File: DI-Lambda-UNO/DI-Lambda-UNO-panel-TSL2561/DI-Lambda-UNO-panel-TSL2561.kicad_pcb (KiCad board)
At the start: 2 copper layers, 33.2 x 26.6 mm, 3 parts, among them J1 Conn_01X06, U1 TSL2561

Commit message: Fix spring contact module name
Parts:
- J1: footprint Sprint-contact-connector-2:Contact-2.5x6 -> Spring-contact-connector-2:Contact-2.5x6
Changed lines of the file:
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@@
     )
   )
-  (module Sprint-contact-connector-2:Contact-2.5x6 (layer F.Cu)
+  (module Spring-contact-connector-2:Contact-2.5x6 (layer F.Cu)
     (at 160 90.7)
     (fp_text reference J1 (at -0.6 0.1) (layer F.SilkS) hide

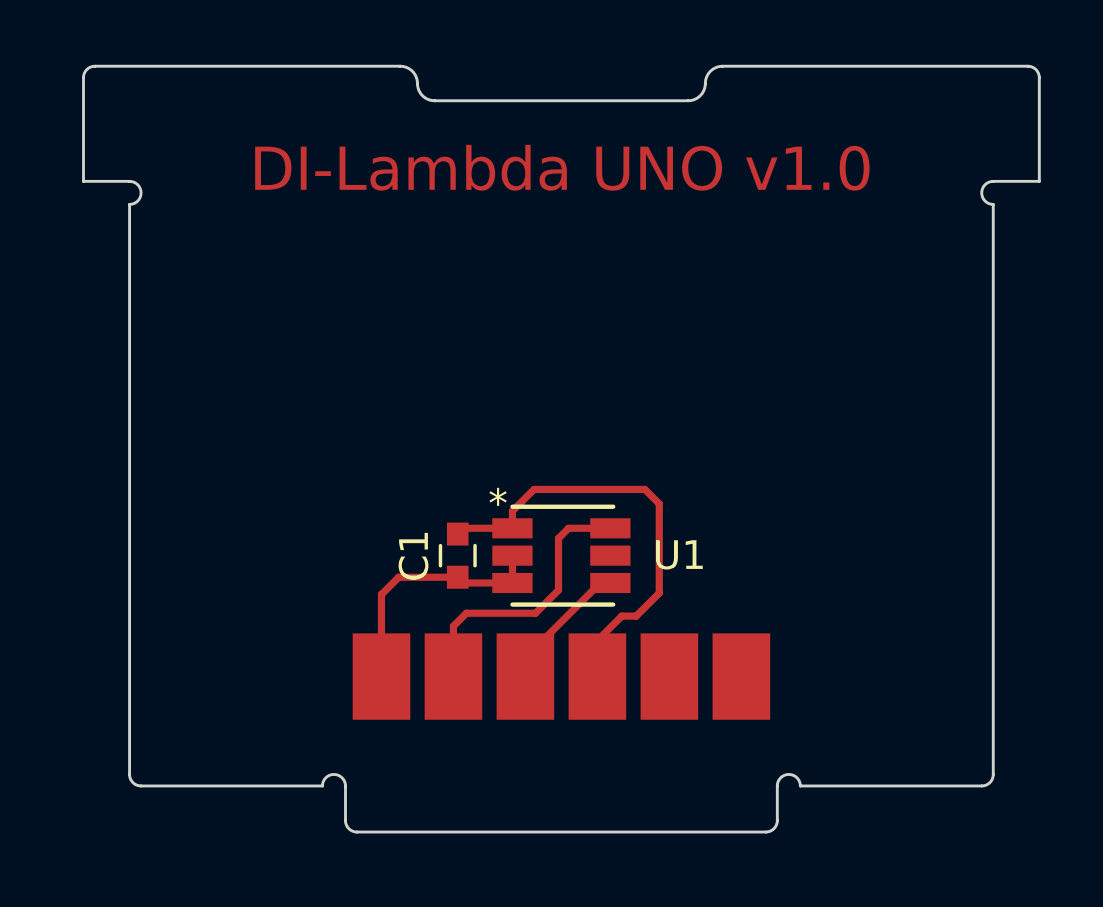
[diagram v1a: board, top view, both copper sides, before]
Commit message: Use longer contact pas for the spring connector
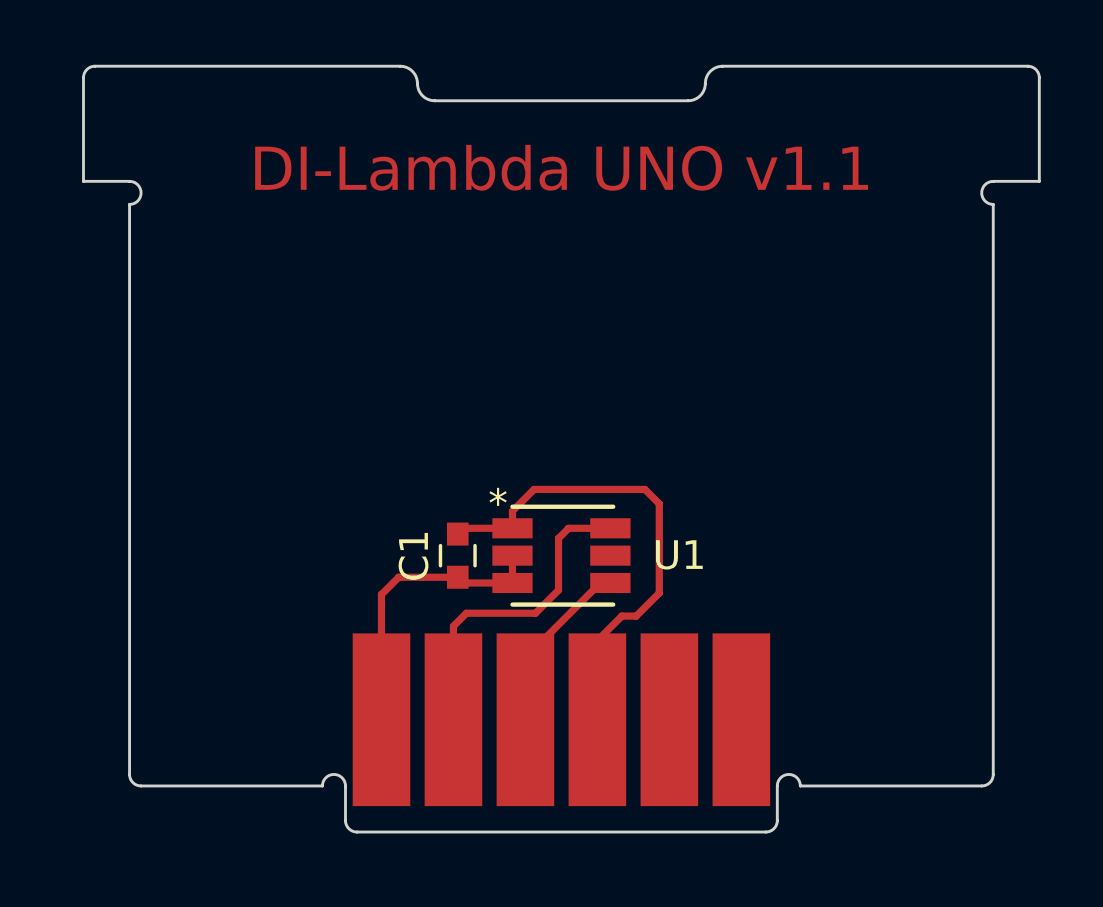
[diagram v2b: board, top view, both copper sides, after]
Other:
- board text added: "DI-Lambda UNO v1.1"
- board text removed: "DI-Lambda UNO v1.0"
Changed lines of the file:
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@@
-(kicad_pcb (version 20170123) (host pcbnew "(2017-07-27 revision 3ee2f80)-test1")
+(kicad_pcb (version 20170123) (host pcbnew "(2017-09-07 revision 3b08636)-master")
   (general
     (thickness 1.6)
@@
       (layerselection 0x000f0_7fffffff)
       (usegerberextensions true)
+      (usegerberattributes true)
+      (usegerberadvancedattributes true)
+      (creategerberjobfile true)
       (excludeedgelayer false)
       (linewidth 0.100000)
@@
     (add_net "Net-(U1-Pad5)")
   )
+  (module Spring-contact-connector-2:Contact-2.5x6 (layer F.Cu)
+    (at 160 90.7)
+    (fp_text reference J1 (at -0.6 0.1) (layer F.SilkS) hide
+      (effects (font (size 1 1) (thickness 0.15)))
+    )
+    (fp_text value Conn_01X06 (at 0 1.5) (layer F.Fab)
+      (effects (font (size 1 1) (thickness 0.15)))
+    )
+    (pad 6 smd rect (at 6.25 -1) (size 2 6) (layers F.Cu F.Paste F.Mask)
+      (net 7 "Net-(J1-Pad6)"))
+    (pad 5 smd rect (at 3.75 -1) (size 2 6) (layers F.Cu F.Paste F.Mask)
+      (net 6 "Net-(J1-Pad5)"))
+    (pad 4 smd rect (at 1.25 -1) (size 2 6) (layers F.Cu F.Paste F.Mask)
+      (net 1 /VCC))
+    (pad 3 smd rect (at -1.25 -1) (size 2 6) (layers F.Cu F.Paste F.Mask)
+      (net 3 /SCL))
+    (pad 2 smd rect (at -3.75 -1) (size 2 6) (layers F.Cu F.Paste F.Mask)
+      (net 5 /SDA))
+    (pad 1 smd rect (at -6.25 -1) (size 2 6) (layers F.Cu F.Paste F.Mask)
+      (net 2 GND))
+  )
   (module Capacitors_SMD:C_0603 (layer F.Cu)
     (at 156.4 84 270)
@@
     )
   )
-  (module Spring-contact-connector-2:Contact-2.5x6 (layer F.Cu)
-    (at 160 90.7)
-    (fp_text reference J1 (at -0.6 0.1) (layer F.SilkS) hide
-      (effects (font (size 1 1) (thickness 0.15)))
-    )
-    (fp_text value Conn_01X06 (at 0 1.5) (layer F.Fab)
-      (effects (font (size 1 1) (thickness 0.15)))
-    )
-    (pad 1 smd rect (at -6.25 -2.5) (size 2 3) (layers F.Cu F.Paste F.Mask)
-      (net 2 GND))
-    (pad 2 smd rect (at -3.75 -2.5) (size 2 3) (layers F.Cu F.Paste F.Mask)
-      (net 5 /SDA))
-    (pad 3 smd rect (at -1.25 -2.5) (size 2 3) (layers F.Cu F.Paste F.Mask)
-      (net 3 /SCL))
-    (pad 4 smd rect (at 1.25 -2.5) (size 2 3) (layers F.Cu F.Paste F.Mask)
-      (net 1 /VCC))
-    (pad 5 smd rect (at 3.75 -2.5) (size 2 3) (layers F.Cu F.Paste F.Mask)
-      (net 6 "Net-(J1-Pad5)"))
-    (pad 6 smd rect (at 6.25 -2.5) (size 2 3) (layers F.Cu F.Paste F.Mask)
-      (net 7 "Net-(J1-Pad6)"))
-  )
   (module TMB:TMB-6 (layer F.Cu)
     (at 160 84)
@@
       (net 5 /SDA))
   )
-  (gr_text "DI-Lambda UNO v1.0" (at 160 70.6) (layer F.Cu)
+  (gr_text "DI-Lambda UNO v1.1" (at 160 70.6) (layer F.Cu)
     (effects (font (size 1.5 1.5) (thickness 0.3)))
   )

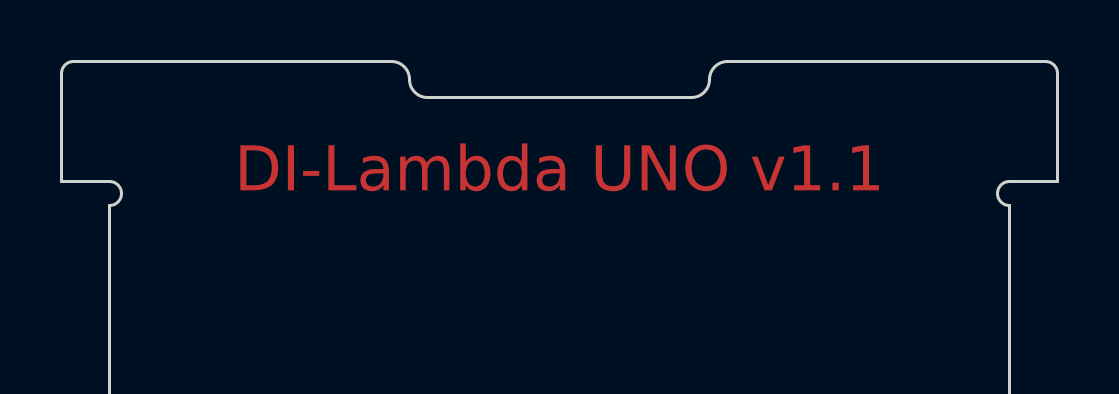
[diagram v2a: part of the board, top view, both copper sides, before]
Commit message: Remove notches from the LED/Sensor/Pinhole panels
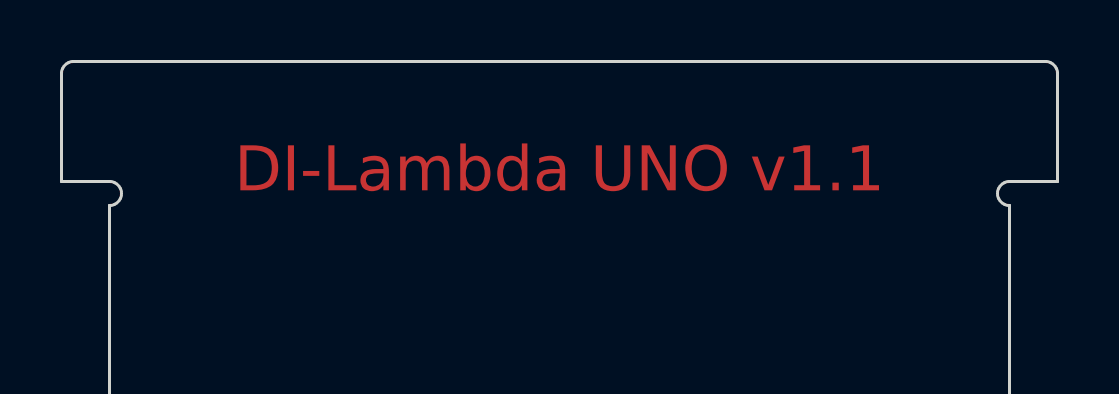
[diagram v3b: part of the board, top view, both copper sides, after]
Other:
- outline, holes or cut-outs redrawn
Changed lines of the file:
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@@
   (general
     (thickness 1.6)
-    (drawings 32)
+    (drawings 26)
     (tracks 27)
     (zones 0)
@@
   (gr_arc (start 167.9 92) (end 167.5 92) (angle 180) (layer Edge.Cuts) (width 0.1))
   (gr_arc (start 152.1 92) (end 151.7 92) (angle 180) (layer Edge.Cuts) (width 0.1))
-  (gr_arc (start 164.4 67.6) (end 165 67.6) (angle 90) (layer Edge.Cuts) (width 0.1))
-  (gr_arc (start 165.6 67.6) (end 165 67.6) (angle 90) (layer Edge.Cuts) (width 0.1))
-  (gr_arc (start 154.4 67.6) (end 154.4 67) (angle 90) (layer Edge.Cuts) (width 0.1))
-  (gr_arc (start 155.6 67.6) (end 155.6 68.2) (angle 90) (layer Edge.Cuts) (width 0.1))
   (gr_line (start 175 91.6) (end 175 71.8) (layer Edge.Cuts) (width 0.1))
-  (gr_line (start 154.4 67) (end 143.8 67) (layer Edge.Cuts) (width 0.1))
+  (gr_line (start 176.2 67) (end 143.8 67) (layer Edge.Cuts) (width 0.1))
   (gr_line (start 175 71) (end 176.6 71) (layer Edge.Cuts) (width 0.1))
   (gr_line (start 145 91.6) (end 145 71.8) (layer Edge.Cuts) (width 0.1))
@@
   (gr_line (start 152.5 92) (end 152.5 93.2) (layer Edge.Cuts) (width 0.1))
   (gr_line (start 145.4 92) (end 151.7 92) (layer Edge.Cuts) (width 0.1))
-  (gr_line (start 176.2 67) (end 165.6 67) (layer Edge.Cuts) (width 0.1))
-  (gr_line (start 155.6 68.2) (end 164.4 68.2) (layer Edge.Cuts) (width 0.1))
   (segment (start 158.3 83.05) (end 158.3 82.45) (width 0.25) (layer F.Cu) (net 1))
   (segment (start 158.3 82.45) (end 159.05 81.7) (width 0.25) (layer F.Cu) (net 1))

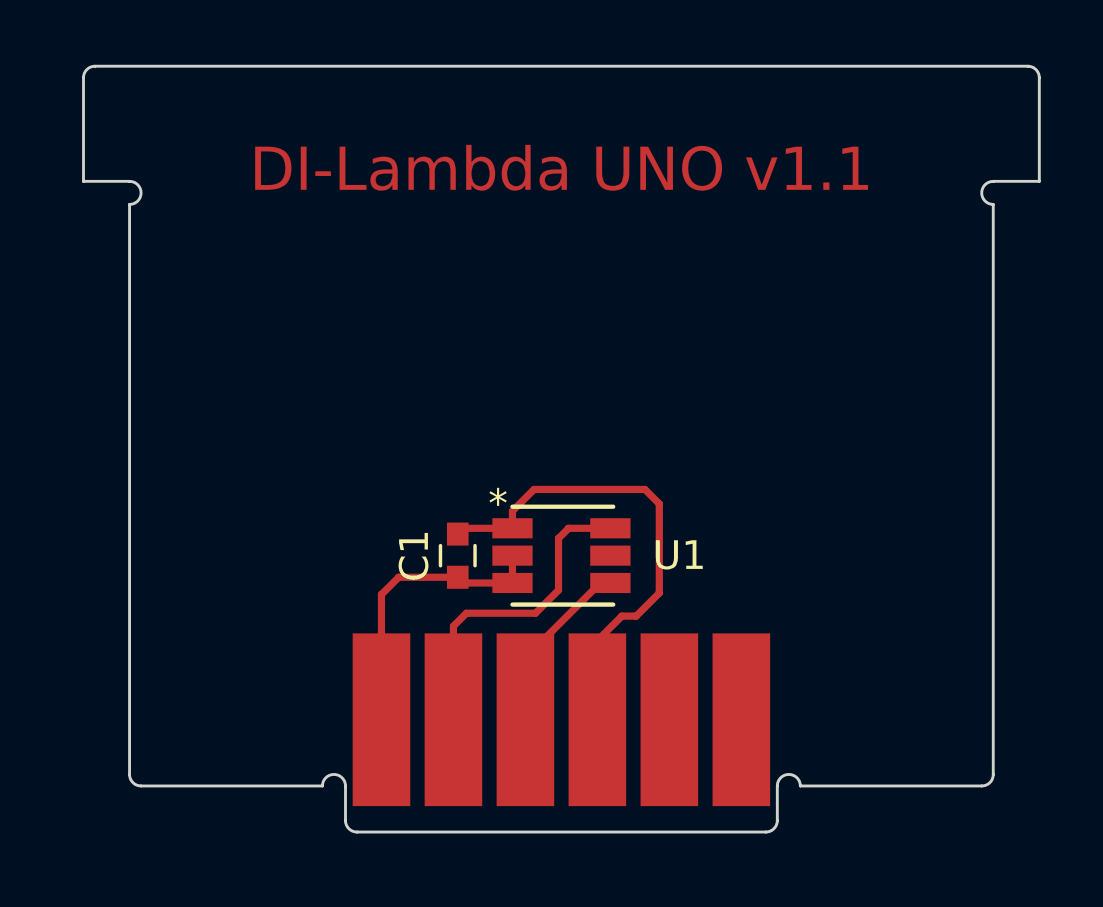
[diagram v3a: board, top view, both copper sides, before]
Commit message: Copper pour and slight dimension adjusements on the TSL5261 board
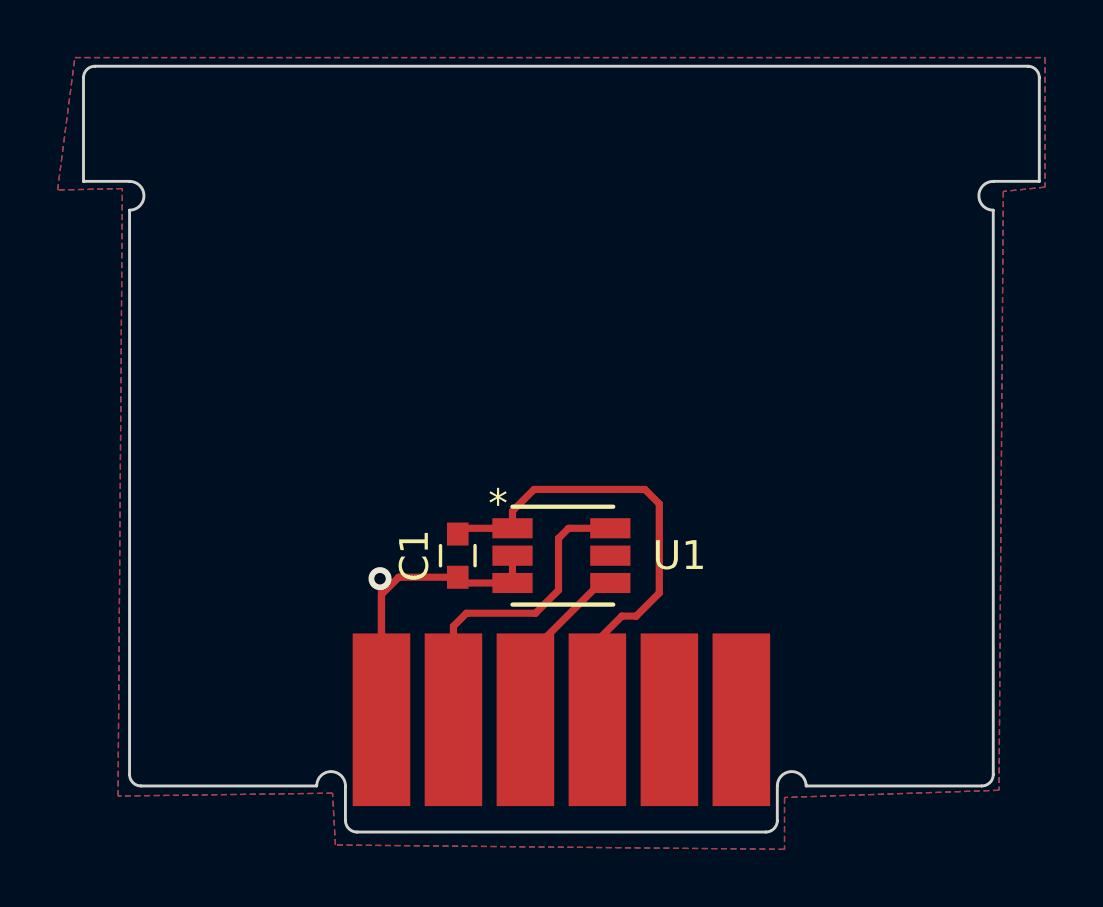
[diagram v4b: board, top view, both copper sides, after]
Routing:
- net GND: track 8.68 -> 13.6 mm, vias 0 -> 1
- added copper zone on B.Cu, net GND
- added copper zone on F.Cu, net GND
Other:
- outline, holes or cut-outs redrawn
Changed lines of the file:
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@@
     (thickness 1.6)
     (drawings 26)
-    (tracks 27)
+    (tracks 30)
     (zones 0)
     (modules 3)
@@
     (40 Dwgs.User user)
     (41 Cmts.User user)
-    (42 Eco1.User user)
+    (42 Eco1.User user hide)
     (43 Eco2.User user)
     (44 Edge.Cuts user)
@@
     (visible_elements FFFFFF7F)
     (pcbplotparams
-      (layerselection 0x000f0_7fffffff)
+      (layerselection 0x010f0_7fffffff)
       (usegerberextensions true)
       (usegerberattributes true)
@@
       (drillshape 0)
       (scaleselection 1)
-      (outputdirectory DI-Lambda-UNO-panel-TSL2561-v1.0-gerbers-20170824/))
+      (outputdirectory DI-Lambda-UNO-panel-TSL2561-v1.0-gerbers-2017oct25/))
   )
   (net 0 "")
@@
       (net 5 /SDA))
   )
-  (gr_text "DI-Lambda UNO v1.1" (at 160 70.6) (layer F.Cu)
+  (gr_text "DI-Lambda UNO v1.1" (at 160 70.6) (layer F.Mask)
     (effects (font (size 1.5 1.5) (thickness 0.3)))
   )
@@
     (arrow2b (pts (xy 152.5 78.9) (xy 153.626504 78.313579)))
   )
-  (gr_arc (start 175 71.4) (end 175 71.8) (angle 180) (layer Edge.Cuts) (width 0.1))
-  (gr_arc (start 145 71.4) (end 145 71) (angle 180) (layer Edge.Cuts) (width 0.1))
+  (gr_arc (start 175 71.5) (end 175 72) (angle 180) (layer Edge.Cuts) (width 0.1))
+  (gr_arc (start 145 71.5) (end 145 71) (angle 180) (layer Edge.Cuts) (width 0.1))
   (gr_arc (start 176.2 67.4) (end 176.2 67) (angle 90) (layer Edge.Cuts) (width 0.1))
   (gr_arc (start 143.8 67.4) (end 143.4 67.4) (angle 90) (layer Edge.Cuts) (width 0.1))
@@
   (gr_arc (start 167.1 93.2) (end 167.5 93.2) (angle 90) (layer Edge.Cuts) (width 0.1))
   (gr_arc (start 152.9 93.2) (end 152.9 93.6) (angle 90) (layer Edge.Cuts) (width 0.1))
-  (gr_arc (start 167.9 92) (end 167.5 92) (angle 180) (layer Edge.Cuts) (width 0.1))
-  (gr_arc (start 152.1 92) (end 151.7 92) (angle 180) (layer Edge.Cuts) (width 0.1))
-  (gr_line (start 175 91.6) (end 175 71.8) (layer Edge.Cuts) (width 0.1))
+  (gr_arc (start 168 92) (end 167.5 92) (angle 180) (layer Edge.Cuts) (width 0.1))
+  (gr_arc (start 152 92) (end 151.5 92) (angle 180) (layer Edge.Cuts) (width 0.1))
+  (gr_line (start 175 91.6) (end 175 72) (layer Edge.Cuts) (width 0.1))
   (gr_line (start 176.2 67) (end 143.8 67) (layer Edge.Cuts) (width 0.1))
   (gr_line (start 175 71) (end 176.6 71) (layer Edge.Cuts) (width 0.1))
-  (gr_line (start 145 91.6) (end 145 71.8) (layer Edge.Cuts) (width 0.1))
-  (gr_line (start 174.6 92) (end 168.3 92) (layer Edge.Cuts) (width 0.1))
+  (gr_line (start 145 91.6) (end 145 72) (layer Edge.Cuts) (width 0.1))
+  (gr_line (start 174.6 92) (end 168.5 92) (layer Edge.Cuts) (width 0.1))
   (gr_line (start 176.6 67.4) (end 176.6 71) (layer Edge.Cuts) (width 0.1))
   (gr_line (start 167.5 93.2) (end 167.5 92) (layer Edge.Cuts) (width 0.1))
@@
   (gr_line (start 145 71) (end 143.4 71) (layer Edge.Cuts) (width 0.1))
   (gr_line (start 152.5 92) (end 152.5 93.2) (layer Edge.Cuts) (width 0.1))
-  (gr_line (start 145.4 92) (end 151.7 92) (layer Edge.Cuts) (width 0.1))
+  (gr_line (start 145.4 92) (end 151.5 92) (layer Edge.Cuts) (width 0.1))
   (segment (start 158.3 83.05) (end 158.3 82.45) (width 0.25) (layer F.Cu) (net 1))
   (segment (start 158.3 82.45) (end 159.05 81.7) (width 0.25) (layer F.Cu) (net 1))
@@
   (segment (start 158.3 83.05) (end 156.6 83.05) (width 0.25) (layer F.Cu) (net 1))
   (segment (start 156.6 83.05) (end 156.4 83.25) (width 0.25) (layer F.Cu) (net 1))
+  (segment (start 153.75 89.7) (end 153.75 84.85) (width 0.25) (layer F.Cu) (net 2))
+  (segment (start 153.75 84.85) (end 153.7 84.8) (width 0.25) (layer F.Cu) (net 2))
+  (via (at 153.7 84.8) (size 0.8) (drill 0.4) (layers F.Cu B.Cu) (net 2))
   (segment (start 158.3 84.95) (end 156.6 84.95) (width 0.25) (layer F.Cu) (net 2))
   (segment (start 156.6 84.95) (end 156.4 84.75) (width 0.25) (layer F.Cu) (net 2))
@@
   (segment (start 156.25 88.2) (end 156.25 86.45) (width 0.25) (layer F.Cu) (net 5))
   (segment (start 156.25 86.45) (end 156.7 86) (width 0.25) (layer F.Cu) (net 5))
+  (zone (net 2) (net_name GND) (layer F.Cu) (hatch edge 0.508)
+    (connect_pads (clearance 0.508))
+    (min_thickness 0.254)
+    (fill yes (arc_segments 16) (thermal_gap 0.508) (thermal_bridge_width 0.508))
+    (polygon
+      (pts
+        (xy 143.1 66.7) (xy 176.8 66.7) (xy 176.8 71.2) (xy 175.35 71.35) (xy 175.2 92.15)
+        (xy 167.75 92.4) (xy 167.75 94.2) (xy 152.15 94.05) (xy 152.05 92.25) (xy 144.6 92.35)
+        (xy 144.75 71.25) (xy 142.5 71.3)
+      )
+    )
+  )
+  (zone (net 2) (net_name GND) (layer B.Cu) (hatch edge 0.508)
+    (connect_pads (clearance 0.508))
+    (min_thickness 0.254)
+    (fill yes (arc_segments 16) (thermal_gap 0.508) (thermal_bridge_width 0.508))
+    (polygon
+      (pts
+        (xy 143.1 66.7) (xy 176.8 66.7) (xy 176.8 71.2) (xy 175.35 71.35) (xy 175.2 92.15)
+        (xy 167.75 92.4) (xy 167.75 94.2) (xy 152.15 94.05) (xy 152.05 92.25) (xy 144.6 92.35)
+        (xy 144.75 71.25) (xy 142.5 71.3)
+      )
+    )
+  )
 )
